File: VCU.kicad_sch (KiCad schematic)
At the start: 50 parts, among them J1 Conn_02x03_Top_Bottom, J2 2x3_Conn, J3 USB_C_Receptacle_USB2.0_14P, J5 Conn_01x02, SW2 SW_Push, SW3 SW_Push, U1 ESP32-S3-WROOM-1, U2 LM1117DT-3.3, U3 SN65HVD230, U4 USBLC6-2SC6, U5 MCP2518FD-xQBB, U6 MCP6001-OT, U7 PTCAN3413DR, Y1 40Mhz Crystal

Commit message: Fix weirdly appearing DRC Issues
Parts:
- removed U2: LM1117DT-3.3, Package_TO_SOT_SMD:TO-252-3_TabPin2, symbol Regulator_Linear:LM1117DT-3.3
- added U8: AP2112K-3.3, Package_TO_SOT_SMD:SOT-23-5, symbol Regulator_Linear:AP2112K-3.3
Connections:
- net +3.3V: now also U8.5 (VOUT)
- net CAN_RX: now also U1.38 (IO2); no longer U1.36 (RXD0)
- net CAN_TX: now also U1.39 (IO1); no longer U1.37 (TXD0)
- net GND: now also U8.2 (GND)
- net IO5: now also U1.26 (IO45); no longer U1.38 (IO2)
- net IO6: now also U1.16 (IO46); no longer U1.39 (IO1)
- net Vin(5V): now also U8.1 (VIN), U8.3 (EN)
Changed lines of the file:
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@@
 	)
 	(junction
-		(at 73.66 182.88)
-		(diameter 0)
-		(color 0 0 0 0)
-	)
-	(junction
 		(at 129.54 179.07)
 		(diameter 0)
@@
 	)
 	(junction
+		(at 58.42 182.88)
+		(diameter 0)
+		(color 0 0 0 0)
+	)
+	(junction
 		(at 264.16 100.33)
 		(diameter 0)
@@
 	)
 	(junction
+		(at 73.66 182.88)
+		(diameter 0)
+		(color 0 0 0 0)
+	)
+	(junction
 		(at 165.1 128.27)
 		(diameter 0)
@@
 	)
 	(no_connect
-		(at 73.66 69.85)
+		(at 63.5 31.75)
 	)
 	(no_connect
-		(at 73.66 72.39)
+		(at 73.66 74.93)
 	)
 	(no_connect
-		(at 73.66 74.93)
+		(at 63.5 34.29)
 	)
 	(no_connect
@@
 	(wire
 		(pts
+			(xy 58.42 182.88) (xy 54.61 182.88)
+		)
+		(stroke
+			(width 0)
+			(type default)
+		)
+	)
+	(wire
+		(pts
 			(xy 22.86 52.07) (xy 33.02 52.07)
 		)
@@
 	(wire
 		(pts
+			(xy 58.42 185.42) (xy 58.42 182.88)
+		)
+		(stroke
+			(width 0)
+			(type default)
+		)
+	)
+	(wire
+		(pts
 			(xy 22.86 39.37) (xy 33.02 39.37)
 		)
@@
 		)
 	)
-	(wire
-		(pts
-			(xy 54.61 182.88) (xy 58.42 182.88)
-		)
-		(stroke
-			(width 0)
-			(type default)
+	(label "IO5"
+		(at 73.66 69.85 0)
+		(effects
+			(font
+				(size 1.27 1.27)
+			)
+			(justify left bottom)
 		)
 	)
@@
 		)
 	)
-	(label "INT"
-		(at 251.46 143.51 0)
+	(label "IO6"
+		(at 73.66 72.39 0)
 		(effects
 			(font
@@
 		)
 	)
-	(label "CANFD+"
-		(at 55.88 157.48 0)
+	(label "INT"
+		(at 251.46 143.51 0)
 		(effects
 			(font
@@
 		)
 	)
-	(label "IO5"
-		(at 22.86 41.91 180)
+	(label "CANFD+"
+		(at 55.88 157.48 0)
 		(effects
 			(font
 				(size 1.27 1.27)
 			)
-			(justify right bottom)
+			(justify left bottom)
 		)
 	)
@@
 		)
 	)
-	(label "IO6"
-		(at 22.86 39.37 180)
-		(effects
-			(font
-				(size 1.27 1.27)
-			)
-			(justify right bottom)
-		)
-	)
 	(label "IO4"
 		(at 73.66 67.31 0)
@@
 		)
 	)
-	(global_label "CAN_TX"
-		(shape output)
-		(at 63.5 31.75 0)
-		(fields_autoplaced yes)
-		(effects
-			(font
-				(size 1.27 1.27)
-			)
-			(justify left)
-		)
-		(property "Intersheetrefs" "${INTERSHEET_REFS}"
-			(at 73.319 31.75 0)
-			(hide yes)
-			(show_name no)
-			(do_not_autoplace no)
-			(effects
-				(font
-					(size 1.27 1.27)
-				)
-				(justify left)
-			)
-		)
-	)
 	(global_label "GPIO2_IN"
 		(shape input)
@@
 		)
 	)
+	(global_label "CAN_RX"
+		(shape output)
+		(at 22.86 41.91 180)
+		(fields_autoplaced yes)
+		(effects
+			(font
+				(size 1.27 1.27)
+			)
+			(justify right)
+		)
+		(property "Intersheetrefs" "${INTERSHEET_REFS}"
+			(at 12.7386 41.91 0)
+			(hide yes)
+			(show_name no)
+			(do_not_autoplace no)
+			(effects
+				(font
+					(size 1.27 1.27)
+				)
+				(justify right)
+			)
+		)
+	)
+	(global_label "CAN_TX"
+		(shape input)
+		(at 22.86 39.37 180)
+		(fields_autoplaced yes)
+		(effects
+			(font
+				(size 1.27 1.27)
+			)
+			(justify right)
+		)
+		(property "Intersheetrefs" "${INTERSHEET_REFS}"
+			(at 13.041 39.37 0)
+			(hide yes)
+			(show_name no)
+			(do_not_autoplace no)
+			(effects
+				(font
+					(size 1.27 1.27)
+				)
+				(justify right)
+			)
+		)
+	)
 	(global_label "BOOTLOAD"
 		(shape input)
@@
 		)
 	)
-	(global_label "CAN_RX"
-		(shape input)
-		(at 63.5 34.29 0)
-		(fields_autoplaced yes)
-		(effects
-			(font
-				(size 1.27 1.27)
-			)
-			(justify left)
-		)
-		(property "Intersheetrefs" "${INTERSHEET_REFS}"
-			(at 73.6214 34.29 0)
-			(hide yes)
-			(show_name no)
-			(do_not_autoplace no)
-			(effects
-				(font
-					(size 1.27 1.27)
-				)
-				(justify left)
-			)
-		)
-	)
 	(global_label "GPIO2_IN"
 		(shape input)
@@
 	)
 	(symbol
-		(lib_id "Regulator_Linear:LM1117DT-3.3")
-		(at 66.04 182.88 0)
-		(unit 1)
-		(body_style 1)
-		(exclude_from_sim no)
-		(in_bom yes)
-		(on_board yes)
-		(in_pos_files yes)
-		(dnp no)
-		(fields_autoplaced yes)
-		(property "Reference" "U2"
-			(at 66.04 176.53 0)
-			(show_name no)
-			(do_not_autoplace no)
-			(effects
-				(font
-					(size 1.27 1.27)
-				)
-			)
-		)
-		(property "Value" "LM1117DT-3.3"
-			(at 66.04 179.07 0)
-			(show_name no)
-			(do_not_autoplace no)
-			(effects
-				(font
-					(size 1.27 1.27)
-				)
-			)
-		)
-		(property "Footprint" "Package_TO_SOT_SMD:TO-252-3_TabPin2"
-			(at 66.04 182.88 0)
-			(hide yes)
-			(show_name no)
-			(do_not_autoplace no)
-			(effects
-				(font
-					(size 1.27 1.27)
-				)
-			)
-		)
-		(property "Datasheet" "http://www.ti.com/lit/ds/symlink/lm1117.pdf"
-			(at 66.04 182.88 0)
-			(hide yes)
-			(show_name no)
-			(do_not_autoplace no)
-			(effects
-				(font
-					(size 1.27 1.27)
-				)
-			)
-		)
-		(property "Description" "800mA Low-Dropout Linear Regulator, 3.3V fixed output, TO-252"
-			(at 66.04 182.88 0)
-			(hide yes)
-			(show_name no)
-			(do_not_autoplace no)
-			(effects
-				(font
-					(size 1.27 1.27)
-				)
-			)
-		)
-		(pin "2"
-		)
-		(pin "3"
-		)
-		(pin "1"
-		)
-		(instances
-			(project "VCU"
-				(path "/be7bcd62-a01d-4d10-b317-838a6e59e497"
-					(reference "U2")
-					(unit 1)
-				)
-			)
-		)
-	)
-	(symbol
 		(lib_id "Device:R_US")
 		(at 105.41 132.08 90)
@@
 	)
 	(symbol
+		(lib_id "Regulator_Linear:AP2112K-3.3")
+		(at 66.04 185.42 0)
+		(unit 1)
+		(body_style 1)
+		(exclude_from_sim no)
+		(in_bom yes)
+		(on_board yes)
+		(in_pos_files yes)
+		(dnp no)
+		(fields_autoplaced yes)
+		(property "Reference" "U8"
+			(at 66.04 176.53 0)
+			(show_name no)
+			(do_not_autoplace no)
+			(effects
+				(font
+					(size 1.27 1.27)
+				)
+			)
+		)
+		(property "Value" "AP2112K-3.3"
+			(at 66.04 179.07 0)
+			(show_name no)
+			(do_not_autoplace no)
+			(effects
+				(font
+					(size 1.27 1.27)
+				)
+			)
+		)
+		(property "Footprint" "Package_TO_SOT_SMD:SOT-23-5"
+			(at 66.04 177.165 0)
+			(hide yes)
+			(show_name no)
+			(do_not_autoplace no)
+			(effects
+				(font
+					(size 1.27 1.27)
+				)
+			)
+		)
+		(property "Datasheet" "https://www.diodes.com/assets/Datasheets/AP2112.pdf"
+			(at 66.04 182.88 0)
+			(hide yes)
+			(show_name no)
+			(do_not_autoplace no)
+			(effects
+				(font
+					(size 1.27 1.27)
+				)
+			)
+		)
+		(property "Description" "600mA low dropout linear regulator, with enable pin, 3.8V-6V input voltage range, 3.3V fixed positive output, SOT-23-5"
+			(at 66.04 185.42 0)
+			(hide yes)
+			(show_name no)
+			(do_not_autoplace no)
+			(effects
+				(font
+					(size 1.27 1.27)
+				)
+			)
+		)
+		(pin "1"
+		)
+		(pin "3"
+		)
+		(pin "2"
+		)
+		(pin "5"
+		)
+		(pin "4"
+		)
+		(instances
+			(project "VCU"
+				(path "/be7bcd62-a01d-4d10-b317-838a6e59e497"
+					(reference "U8")
+					(unit 1)
+				)
+			)
+		)
+	)
+	(symbol
 		(lib_id "power:GND")
 		(at 251.46 106.68 180)
@@
 	(symbol
 		(lib_id "power:GND")
-		(at 66.04 190.5 0)
+		(at 66.04 193.04 0)
 		(unit 1)
 		(body_style 1)
@@
 		(fields_autoplaced yes)
 		(property "Reference" "#PWR04"
-			(at 66.04 196.85 0)
+			(at 66.04 199.39 0)
 			(hide yes)
 			(show_name no)
@@
 		)
 		(property "Value" "GND"
-			(at 66.04 195.58 0)
+			(at 66.04 198.12 0)
 			(show_name no)
 			(do_not_autoplace no)
@@
 		)
 		(property "Footprint" ""
-			(at 66.04 190.5 0)
+			(at 66.04 193.04 0)
 			(hide yes)
 			(show_name no)
@@
 		)
 		(property "Datasheet" ""
-			(at 66.04 190.5 0)
+			(at 66.04 193.04 0)
 			(hide yes)
 			(show_name no)
@@
 		)
 		(property "Description" "Power symbol creates a global label with name \"GND\" , ground"
-			(at 66.04 190.5 0)
+			(at 66.04 193.04 0)
 			(hide yes)
 			(show_name no)

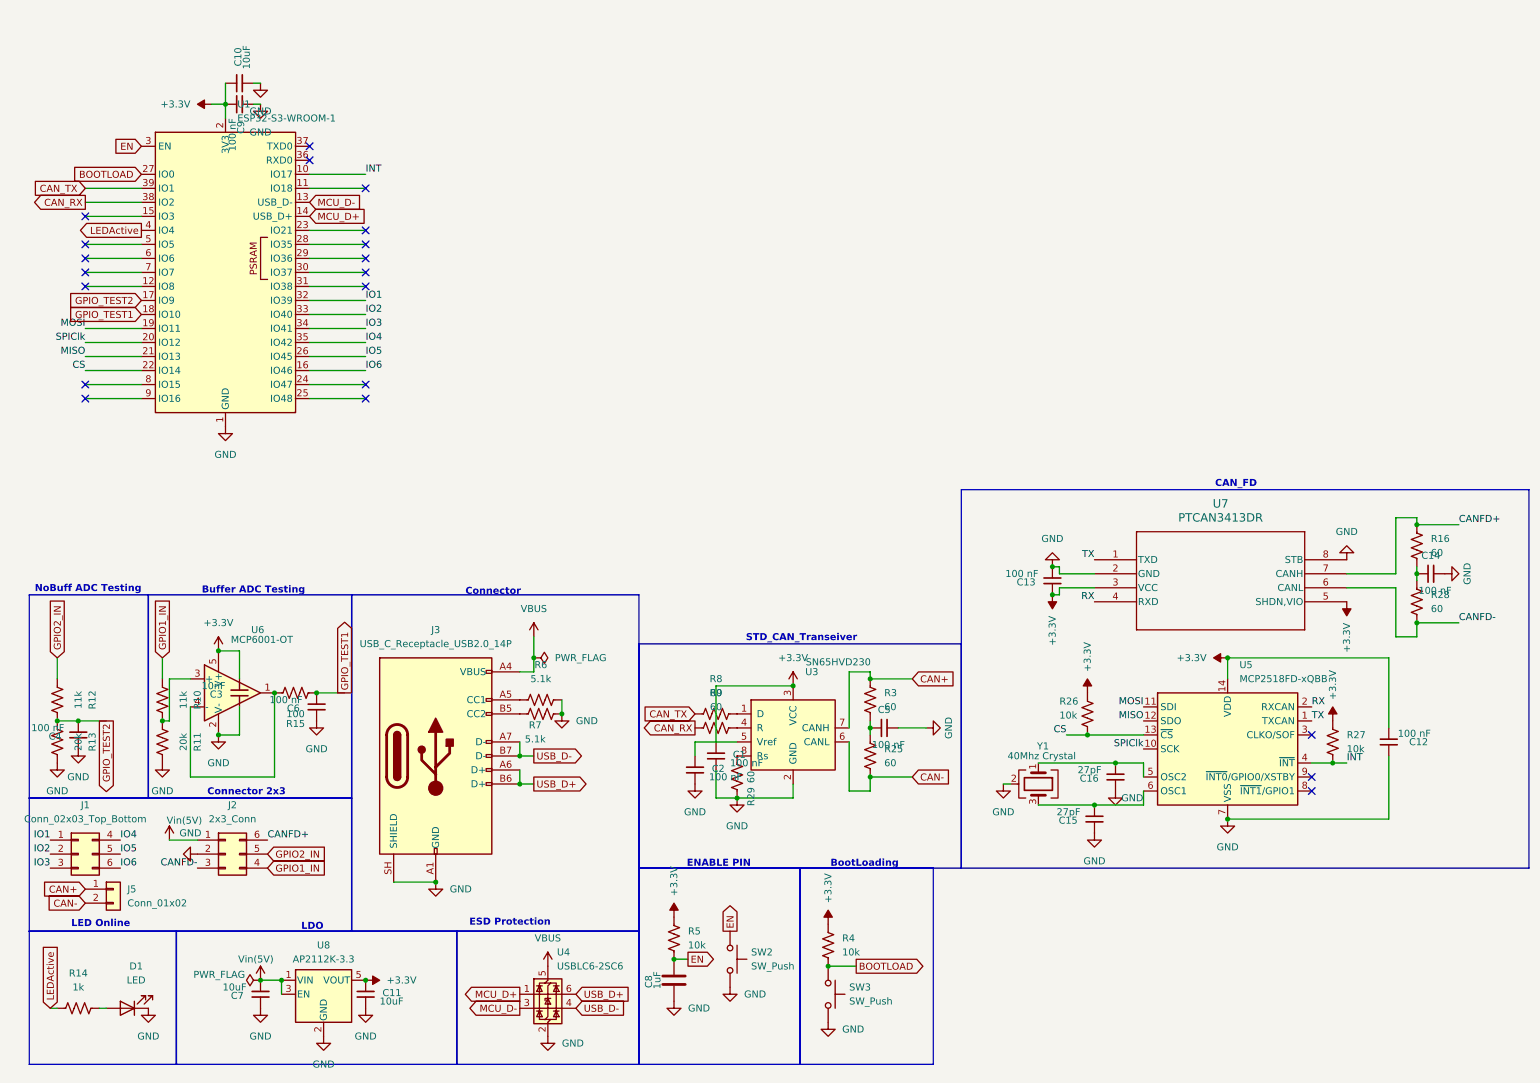
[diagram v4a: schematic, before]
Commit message: Add bom
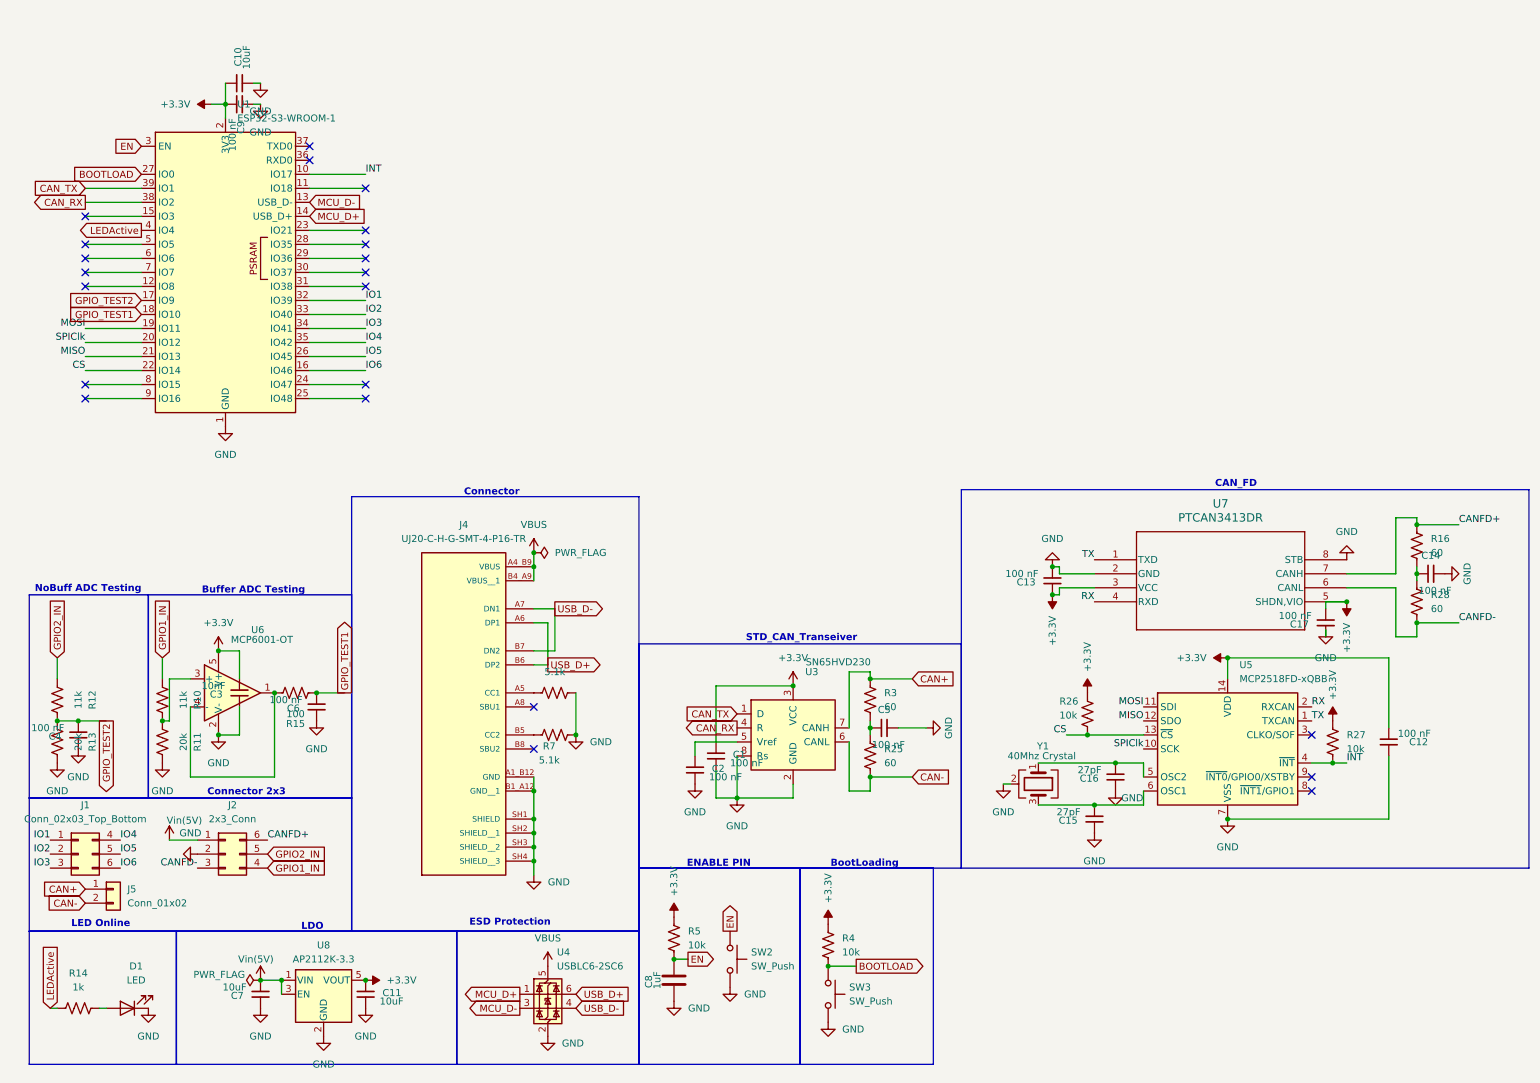
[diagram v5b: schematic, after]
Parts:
- removed J3: USB_C_Receptacle_USB2.0_14P, SK's_Components:USB_C_HRO_TYPE-C-31-M-14, symbol Connector:USB_C_Receptacle_USB2.0_14P
- removed R29, R8, R9: 60, Resistor_SMD:R_0805_2012Metric, symbol Device:R_US
- added C17: 100 nF, Capacitor_SMD:C_0805_2012Metric, symbol Device:C_Small
- added J4: UJ20-C-H-G-SMT-4-P16-TR, UJ20-C-H-G-SMT-4-P16-TR:SAMESKY_UJ20-C-H-G-SMT-4-P16-TR, symbol UJ20-C-H-G-SMT-4-P16-TR:UJ20-C-H-G-SMT-4-P16-TR
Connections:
- net +3.3V: now also C17.2
- net CAN_RX: now also U3.4 (R)
- net CAN_TX: now also U3.1 (D)
- net GND: now also U3.8 (Rs), C17.1, J4.A1_B12 (GND), J4.B1_A12 (GND__1), J4.SH1 (SHIELD), J4.SH2 (SHIELD__1), J4.SH3 (SHIELD__2), J4.SH4 (SHIELD__3)
- net USB_D+: now also J4.A6 (DP1), J4.B6 (DP2)
- net USB_D-: now also J4.A7 (DN1), J4.B7 (DN2)
- net VBUS: now also J4.A4_B9 (VBUS), J4.B4_A9 (VBUS__1)
- net at R6.1: now also J4.A5 (CC1)
- net at R7.1: now also J4.B5 (CC2)
- no-connect marks 20 -> 22
